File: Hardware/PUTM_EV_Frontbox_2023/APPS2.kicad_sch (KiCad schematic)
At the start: 23 parts, among them U22 MCP6N11-005, U23 MCP6001

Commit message: Started PCB layout
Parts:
- removed C55, C56, C59, C60: 100n, Capacitor_SMD:C_0603_1608Metric_Pad1.08x0.95mm_HandSolder, symbol Device:C_Small
- removed C57, C58: 10n, Capacitor_SMD:C_0603_1608Metric_Pad1.08x0.95mm_HandSolder, symbol Device:C_Small
- removed D10: 24V, Diode_SMD:D_0603_1608Metric_Pad1.05x0.95mm_HandSolder, symbol Device:D_TVS
- removed JP4: POT/DAC, Jumper:SolderJumper-3_P1.3mm_Bridged12_RoundedPad1.0x1.5mm, symbol Jumper:SolderJumper_3_Bridged12
- removed R75: 10k, Resistor_SMD:R_0603_1608Metric_Pad0.98x0.95mm_HandSolder, symbol Device:R_Small
- removed R78: 33k, Resistor_SMD:R_0603_1608Metric_Pad0.98x0.95mm_HandSolder, symbol Device:R_Small
- removed R90: 100k, Resistor_SMD:R_0603_1608Metric_Pad0.98x0.95mm_HandSolder, symbol Device:R_Small
- removed R91: 0R, Resistor_SMD:R_0603_1608Metric_Pad0.98x0.95mm_HandSolder, symbol Device:R_Small
- removed R92, R94, R95: 4k7, Resistor_SMD:R_0603_1608Metric_Pad0.98x0.95mm_HandSolder, symbol Device:R_Small
- removed R93: 1k, Resistor_SMD:R_0603_1608Metric_Pad0.98x0.95mm_HandSolder, symbol Device:R_Small
- removed RV7: 1k, Potentiometer_SMD:Potentiometer_Bourns_3214J_Horizontal, symbol Device:R_Potentiometer_Small
- removed TP30: APPS_P, TestPoint:TestPoint_Pad_D1.0mm, symbol Connector:TestPoint
- removed TP31: APPS_N, TestPoint:TestPoint_Pad_D1.0mm, symbol Connector:TestPoint
- removed TP32: APPS_MID, TestPoint:TestPoint_Pad_D1.0mm, symbol Connector:TestPoint
- removed TP33: APPS_OUT, TestPoint:TestPoint_Pad_D1.0mm, symbol Connector:TestPoint
- removed U22: MCP6N11-005, Package_DFN_QFN:TDFN-8-1EP_3x2mm_P0.5mm_EP1.3x1.4mm, symbol MCP6N11:MCP6N11
- removed U23: MCP6001, Package_TO_SOT_SMD:SOT-23-5, symbol Amplifier_Operational:MCP6001-OT
- added C49, C50, C53, C54: 100n, Capacitor_SMD:C_0603_1608Metric_Pad1.08x0.95mm_HandSolder, symbol Device:C_Small
- added C51, C52: 10n, Capacitor_SMD:C_0603_1608Metric_Pad1.08x0.95mm_HandSolder, symbol Device:C_Small
- added D9: 24V, Diode_SMD:D_0603_1608Metric_Pad1.05x0.95mm_HandSolder, symbol Device:D_TVS
- added JP3: POT/DAC, Jumper:SolderJumper-3_P1.3mm_Bridged12_RoundedPad1.0x1.5mm, symbol Jumper:SolderJumper_3_Bridged12
- added R67: 10k, Resistor_SMD:R_0603_1608Metric_Pad0.98x0.95mm_HandSolder, symbol Device:R_Small
- added R68: 33k, Resistor_SMD:R_0603_1608Metric_Pad0.98x0.95mm_HandSolder, symbol Device:R_Small
- added R69: 100k, Resistor_SMD:R_0603_1608Metric_Pad0.98x0.95mm_HandSolder, symbol Device:R_Small
- added R70: 0R, Resistor_SMD:R_0603_1608Metric_Pad0.98x0.95mm_HandSolder, symbol Device:R_Small
- added R71, R73, R74: 4k7, Resistor_SMD:R_0603_1608Metric_Pad0.98x0.95mm_HandSolder, symbol Device:R_Small
- added R72: 1k, Resistor_SMD:R_0603_1608Metric_Pad0.98x0.95mm_HandSolder, symbol Device:R_Small
- added RV6: 1k, Potentiometer_SMD:Potentiometer_Bourns_3214J_Horizontal, symbol Device:R_Potentiometer_Small
- added TP26: APPS_P, TestPoint:TestPoint_Pad_D1.0mm, symbol Connector:TestPoint
- added TP27: APPS_N, TestPoint:TestPoint_Pad_D1.0mm, symbol Connector:TestPoint
- added TP28: APPS_MID, TestPoint:TestPoint_Pad_D1.0mm, symbol Connector:TestPoint
- added TP29: APPS_OUT, TestPoint:TestPoint_Pad_D1.0mm, symbol Connector:TestPoint
- added U18: MCP6N11-005, Package_DFN_QFN:TDFN-8-1EP_3x2mm_P0.5mm_EP1.3x1.4mm, symbol MCP6N11:MCP6N11
- added U21: MCP6001, Package_TO_SOT_SMD:SOT-23-5, symbol Amplifier_Operational:MCP6001-OT
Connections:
- net GND: now also C49.2, C50.2, C51.2, C52.2, C53.2, D9.1 (A1), R68.2, R69.2, R72.1, U18.4 (V-), U18.5 (RF), U18.9 (EP), U21.2 (V-)
- net OUT1: now also C54.2, TP29.1, U21.1, U21.4 (-)
- new net: R71.2, R73.1, TP28.1, U18.6
- new net: R68.1, RV6.3
- new net: R70.1, U18.8 (EN)
- new net: R71.1, R72.2, U18.1 (FG)
- new net: C54.1, R73.2, R74.1
- new net: C53.1, R74.2, U21.3 (+)
- new net: JP3.2 (C), TP27.1, U18.2 (-)
- new net: C51.1, JP3.3 (B), RV6.2
- new net: R67.2, RV6.1
- new net 3V3_POT1: C49.1, C50.1, R67.1, R70.2, U18.7 (V+), U21.5 (V+)
- new net DAC_REF1: C52.1, JP3.1 (A)
- new net POT1: D9.2 (A2), R69.1, TP26.1, U18.3 (+)

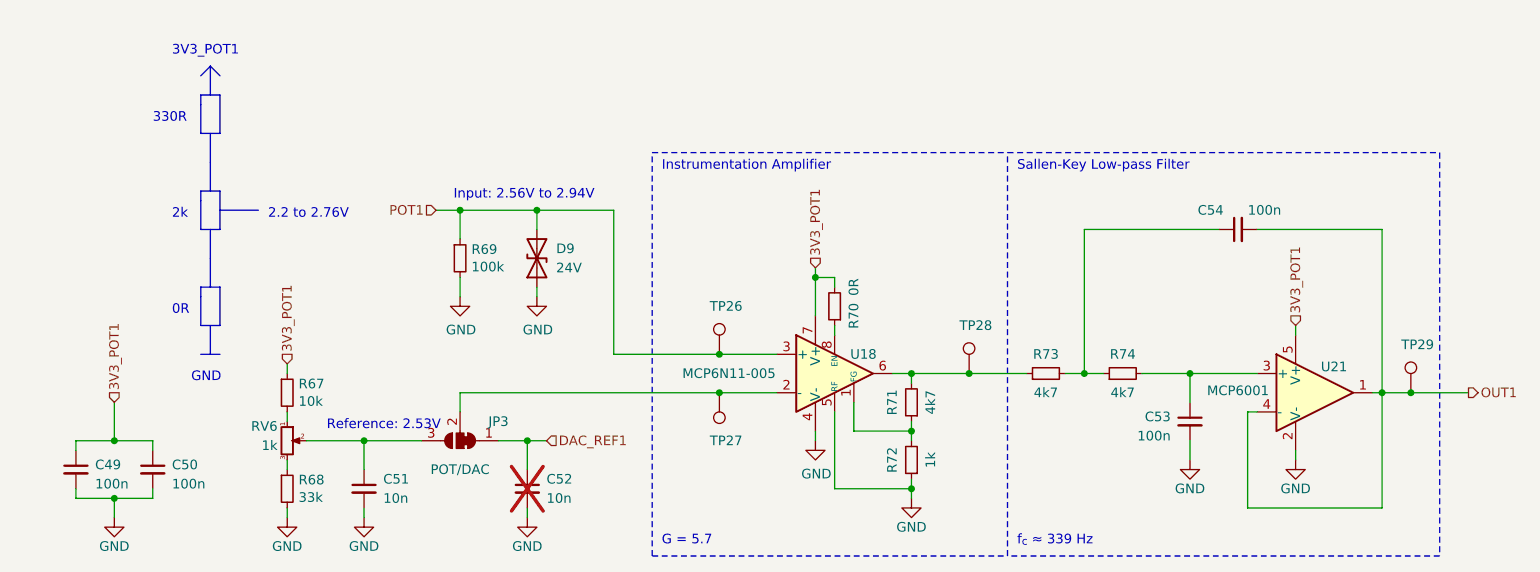
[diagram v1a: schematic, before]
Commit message: Removed APPS pots
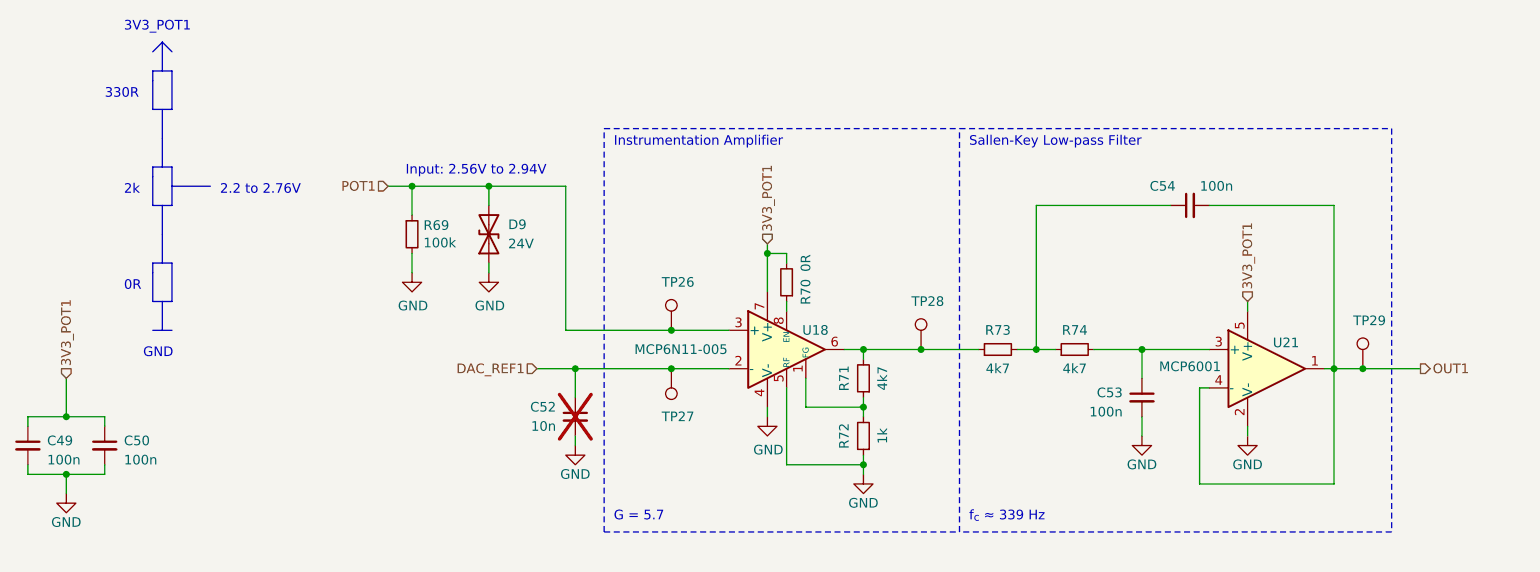
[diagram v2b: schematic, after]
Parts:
- removed C51: 10n, Capacitor_SMD:C_0603_1608Metric_Pad1.08x0.95mm_HandSolder, symbol Device:C_Small
- removed JP3: POT/DAC, Jumper:SolderJumper-3_P1.3mm_Bridged12_RoundedPad1.0x1.5mm, symbol Jumper:SolderJumper_3_Bridged12
- removed R67: 10k, Resistor_SMD:R_0603_1608Metric_Pad0.98x0.95mm_HandSolder, symbol Device:R_Small
- removed R68: 33k, Resistor_SMD:R_0603_1608Metric_Pad0.98x0.95mm_HandSolder, symbol Device:R_Small
- removed RV6: 1k, Potentiometer_SMD:Potentiometer_Bourns_3214J_Horizontal, symbol Device:R_Potentiometer_Small
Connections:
- net DAC_REF1: now also TP27.1, U18.2 (-)
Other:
- note removed: "Reference: 2.53V"
- moved on the sheet: C49, C50, C52, C53, C54, D9, R69, R70, R71, R72, R73, R74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
